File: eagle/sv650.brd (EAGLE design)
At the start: 54.2 x 52 mm, 28 parts, among them Q1 IRLML6344

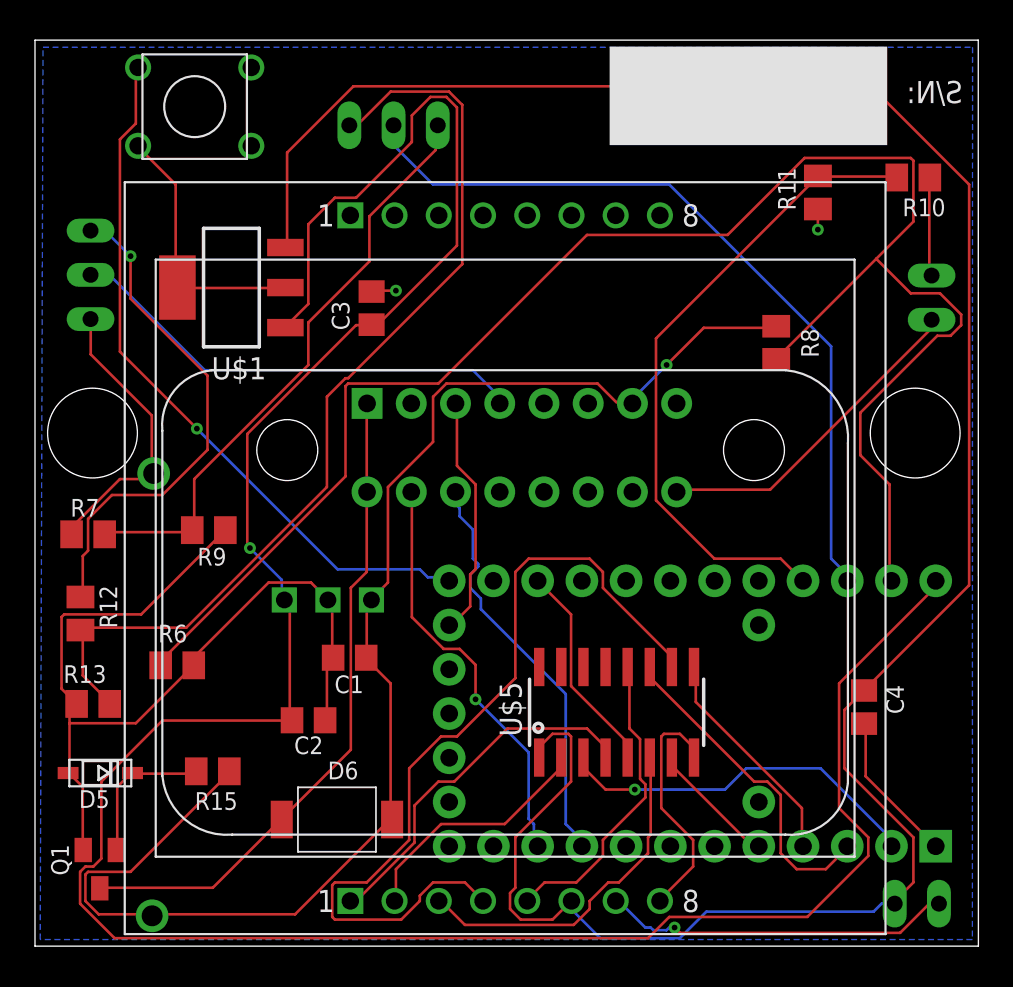
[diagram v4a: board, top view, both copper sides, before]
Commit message: v5.0 board with Nokia 5110 LCD screen
as ordered from OSHPark
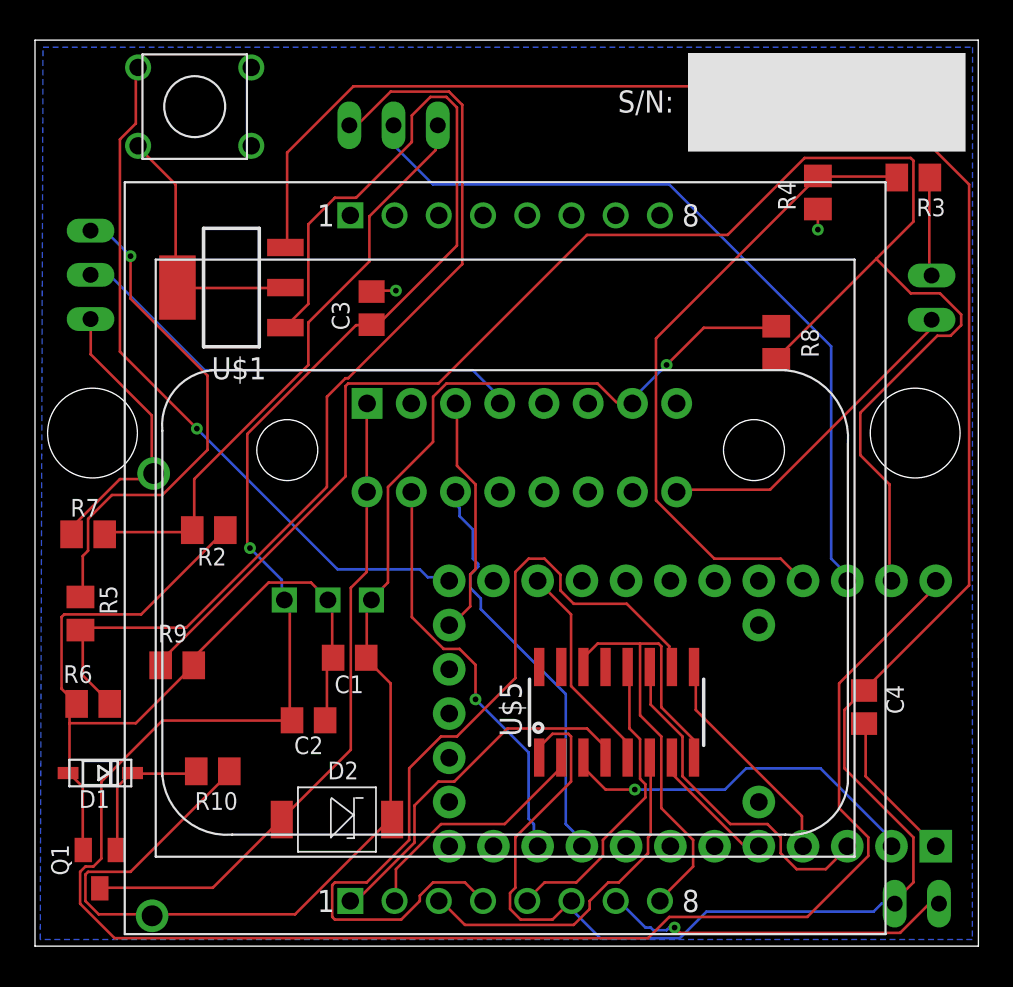
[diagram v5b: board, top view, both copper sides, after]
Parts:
- removed R12: 30k, resistor:M0805
- removed R13, R15: 13.3k, resistor:M0805
- added R1: 82, synfinatic:AXIAL-0.9
- added R2: 13.3k, resistor:M0805
- added R3: 30K, resistor:M0805
- R10: value 30K -> 13.3k
- R5: value 82 -> 30k; device synfinatic:AXIAL-0.9 -> resistor:M0805
- moved R10 52.7 mm to (10.2, 10.0), turned to 0 degrees
- moved R9 7.97 mm to (8.17, 16.1)
- moved R5 5.88 mm to (2.61, 19.1), flipped to the top, turned to 270 degrees
- moved R6 5.31 mm to (3.34, 13.9), turned to 0 degrees
- renumbered D5 to D1, D6 to D2, R11 to R4
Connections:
- net +12V: now also R1.P$2, R10.2; no longer R15.2, R5.P$2
- net BATTMON: now also R9.2; no longer R6.2
- net FUEL2: now also R3.1; no longer R10.1
- net FUEL2_ADC: now also R3.2; no longer R10.2
- net FUEL_A: now also R1.P$1; no longer R5.P$1
- net FUEL_A_ADC: now also R2.2; no longer R9.2
- net FUEL_B: now also R5.1; no longer R12.1
- net FUEL_B_ADC: now also R5.2, R6.2; no longer R12.2, R13.2
- net GND: now also R2.1, U$5.14; no longer R13.1
- net N$17: now also R10.1; no longer R15.1
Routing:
- net GND: track 92.3 -> 107.9 mm
- net CLK: track 19.1 -> 19.9 mm
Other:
- board text added: "20150425"
- board text added: "https://synfin.net/sv650ecu SV650 ECU Decoder v5.0"
- board text removed: "20150423"
- board text removed: "http://synfin.net/sv650ecu SV650 ECU Decoder v5.0"
